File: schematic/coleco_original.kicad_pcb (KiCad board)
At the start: 2 copper layers, 168.4 x 318 mm, 220 parts, among them J0 Conn_01x04, J1 Cartridge Port, J2 Expansion Port, J4A1 Conn_01x08, J4B1 Conn_01x08, J5 DB9_Male, J6 DB9_Male, Q2 2N3906, Q3 2N3906, Q4 2N3904, Q5 2N3904, Q6 2N3906, U1 Z80CPU, U10 MK4116P, U11 MK4116P, U12 MK4116P, U13 MK4116P, U14 MK4116P, U15 MK4116P, U16 MK4116P, U17 MK4116P, U18 74LS541, U19 74LS541, U2 27C256, U20 SN76489AN, U22 74LS04, U23 4066, U24 74LS00, U3 SCM2114AL, U4 SCM2114AL, U5 74LS138, U6 74LS138, U7 74LS05, U8 74LS74, U9 TMS9928A, Y1 7.159090Mhz

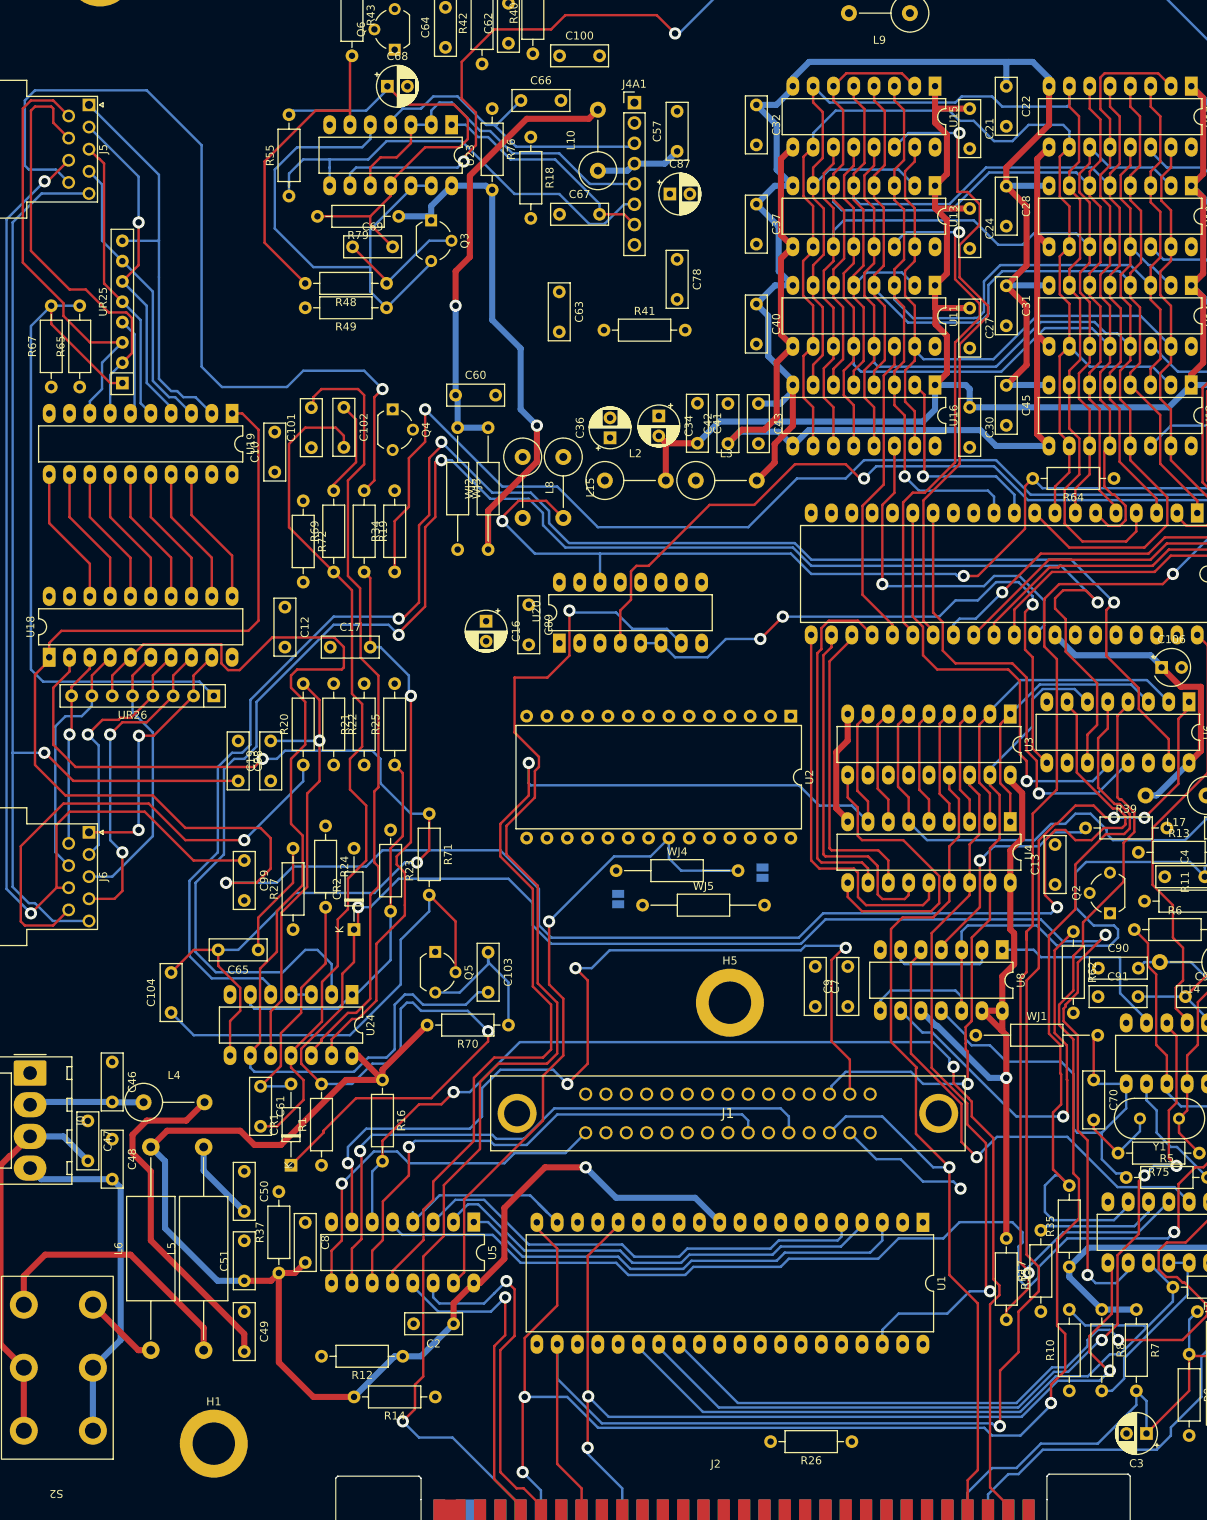
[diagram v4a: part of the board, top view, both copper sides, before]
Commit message: added memory, eprom and sound lines. some video as well. fixed the cap size for polar. its a bit weird since they use 5 mm pin and 5mm body and bend out the leads.
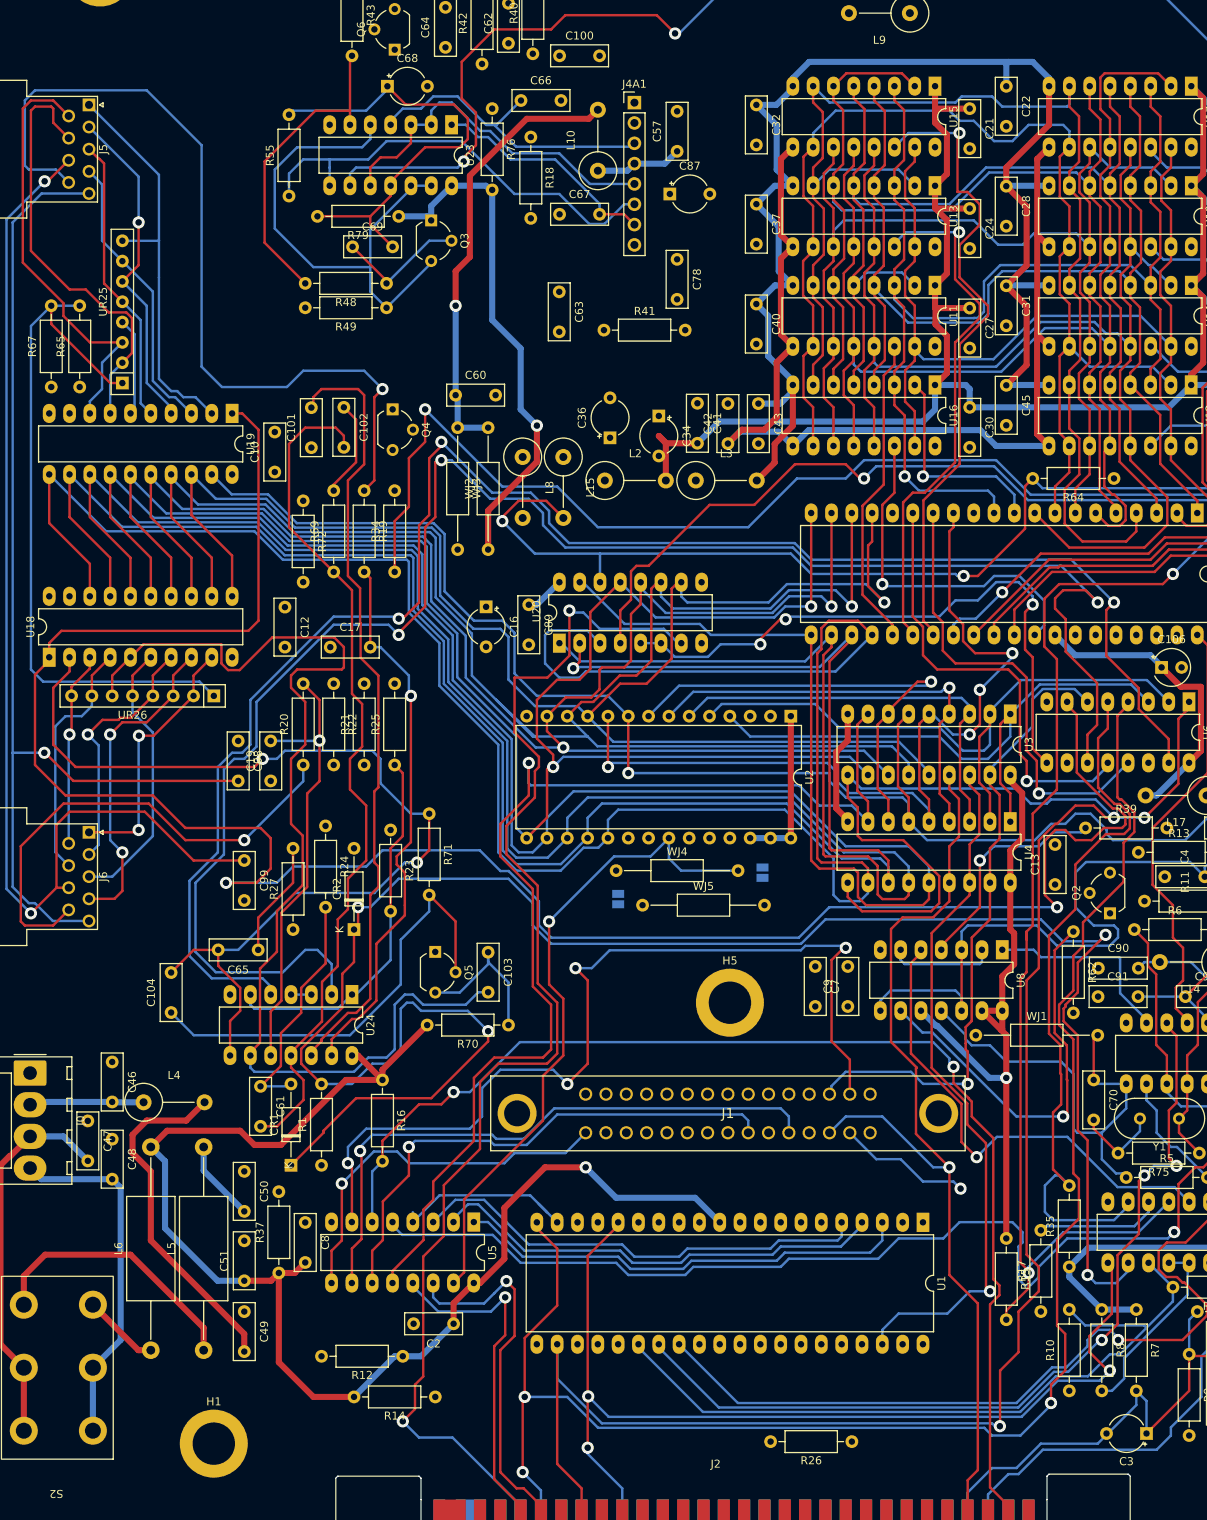
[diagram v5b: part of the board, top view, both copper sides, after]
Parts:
- C16, C3, C34, C36, C68, C87: footprint Capacitor_THT:CP_Radial_D5.0mm_P2.50mm -> Capacitor_THT:CP_Radial_Tantal_D4.5mm_P5.00mm
- moved C16 1.80 mm to (115.6, 120.3)
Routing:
- net /cpu/D7: track 62.4 -> 268.8 mm
- net /cpu/D3: track 17.3 -> 219.2 mm, vias 0 -> 2
- net /cpu/D1: track 17.3 -> 207.6 mm, vias 0 -> 1
- net /cpu/D6: track 55.9 -> 243.3 mm, vias 0 -> 1
- net /cpu/D2: track 17.3 -> 201.3 mm, vias 0 -> 2
- net /cpu/D5: track 62.0 -> 245.6 mm
- net /cpu/D0: track 17.3 -> 198.2 mm, vias 0 -> 1
- net /cpu/D4: track 66.7 -> 245.6 mm
- net /cpu/A1: track 138.9 -> 257.3 mm, vias 1 -> 2
- net /cpu/A0: track 14.5 -> 108.0 mm, vias 0 -> 4
- net /cpu/A2: track 14.6 -> 58.9 mm, vias 0 -> 1
- net /cpu/A5: track 40.0 -> 82.3 mm
- net /cpu/A6: track 34.2 -> 75.4 mm
- net /cpu/A3: track 14.5 -> 54.3 mm, vias 0 -> 1
- net /cpu/A4: track 14.5 -> 51.9 mm
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
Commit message: working on eeprom, cart port, cpu
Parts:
- moved C9 4.49 mm to (160.8, 165.8), turned to -90 degrees
- moved C34 3.36 mm to (136.7, 93.1)
- moved C36 2.29 mm to (129.0, 98.1)
- moved C7 0.51 mm to (156.7, 165.8)
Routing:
- net /cpu/~{NMI}: track 0.00 -> 191.8 mm, vias 0 -> 4
- net /cpu/D1: track 207.6 -> 322.1 mm
- net /cpu/D0: track 198.2 -> 310.3 mm
- net /cpu/D7: track 268.8 -> 366.2 mm, vias 0 -> 1
- net /cpu/~{HALT}: track 0.00 -> 77.1 mm
- net /cpu/A3: track 54.3 -> 110.5 mm
- net /cpu/A4: track 51.9 -> 106.6 mm
- net /cpu/A7: track 80.2 -> 133.9 mm
- net /cpu/A6: track 75.4 -> 127.9 mm
- net /cpu/A5: track 82.3 -> 134.6 mm
- net /cpu/A2: track 58.9 -> 109.2 mm
- net /cpu/D2: track 201.3 -> 251.3 mm
- net /cpu/D3: track 219.2 -> 268.3 mm
- net /cpu/A1: track 257.3 -> 302.6 mm
- net /cpu/A0: track 108.0 -> 153.2 mm
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
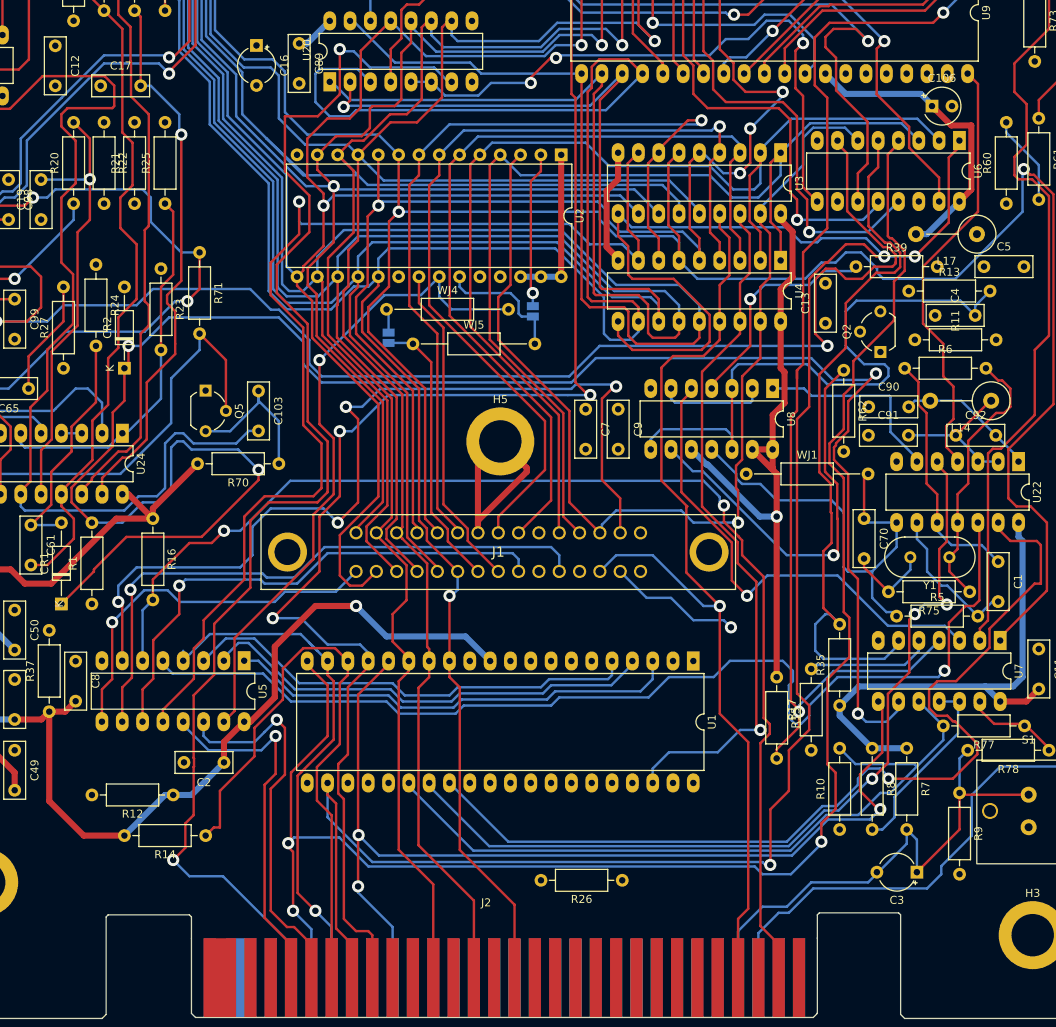
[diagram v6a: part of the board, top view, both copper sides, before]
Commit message: most of the semi-conductors are done.
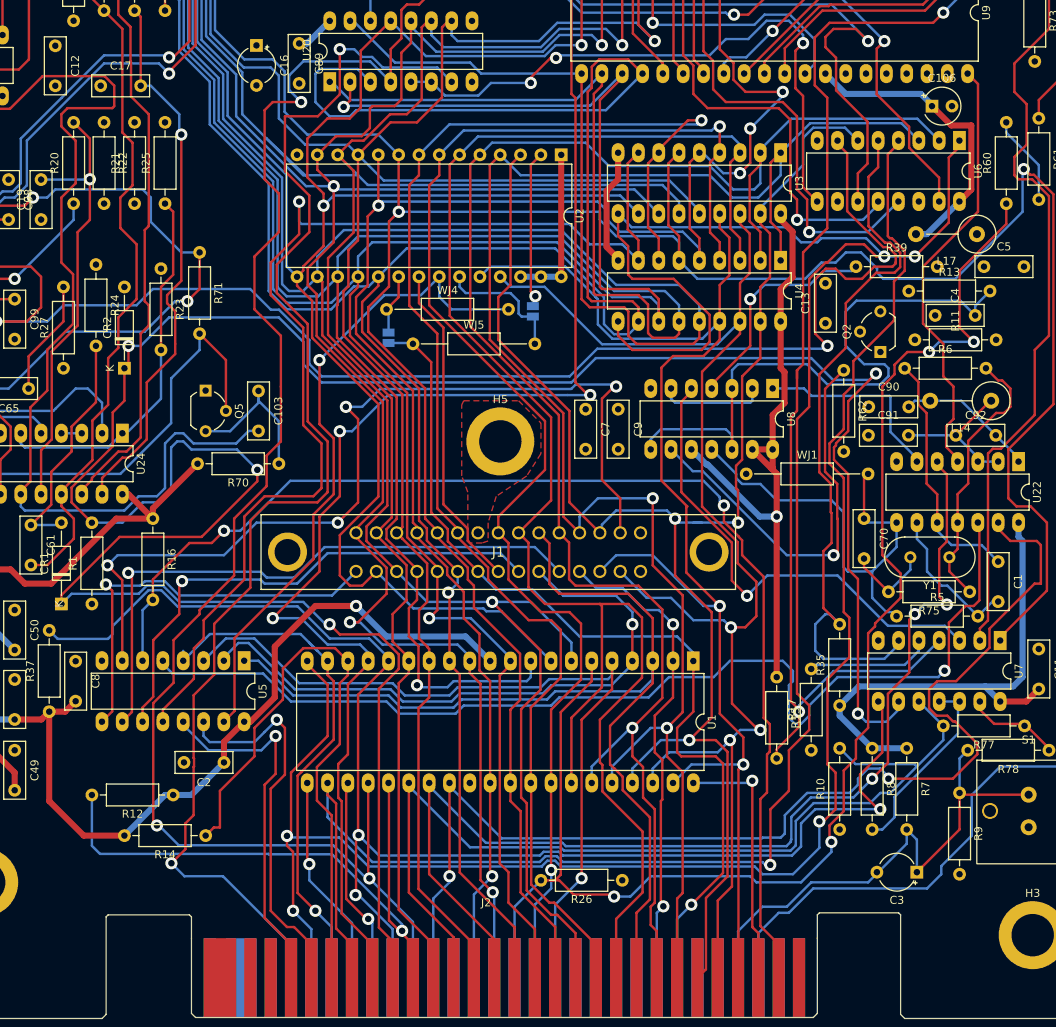
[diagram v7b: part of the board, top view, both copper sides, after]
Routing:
- net /clock_reset_misc_logic/~{CLK}: track 0.00 -> 181.2 mm, vias 0 -> 4
- net /clock_reset_misc_logic/~{WAIT}: track 237.2 -> 416.2 mm, vias 3 -> 6
- net /cpu/A4: track 106.6 -> 204.5 mm
- net /clock_reset_misc_logic/INT: track 244.1 -> 333.2 mm, vias 4 -> 5
- net /cpu/A6: track 127.9 -> 214.3 mm, vias 0 -> 2
- net /cpu/D4: track 288.7 -> 370.3 mm, vias 0 -> 1
- net /cpu/A11: track 34.9 -> 114.8 mm, vias 0 -> 1
- net /cpu/A5: track 134.6 -> 212.6 mm, vias 0 -> 1
- net /cpu/A7: track 133.9 -> 211.2 mm, vias 1 -> 3
- net /cpu/~{BUSRQ}: track 0.00 -> 76.0 mm, vias 0 -> 1
- net /cpu/D2: track 251.3 -> 324.7 mm, vias 2 -> 4
- net /cpu/A13: track 57.2 -> 128.8 mm
- net /cpu/A8: track 104.5 -> 174.3 mm, vias 2 -> 3
- net /cpu/A2: track 109.2 -> 177.1 mm
- net /cpu/A3: track 110.5 -> 174.9 mm, vias 1 -> 2
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- added copper zone on F.Cu, net GND
